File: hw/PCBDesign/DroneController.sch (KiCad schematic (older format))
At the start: 5 parts, among them J1 SerialDebug

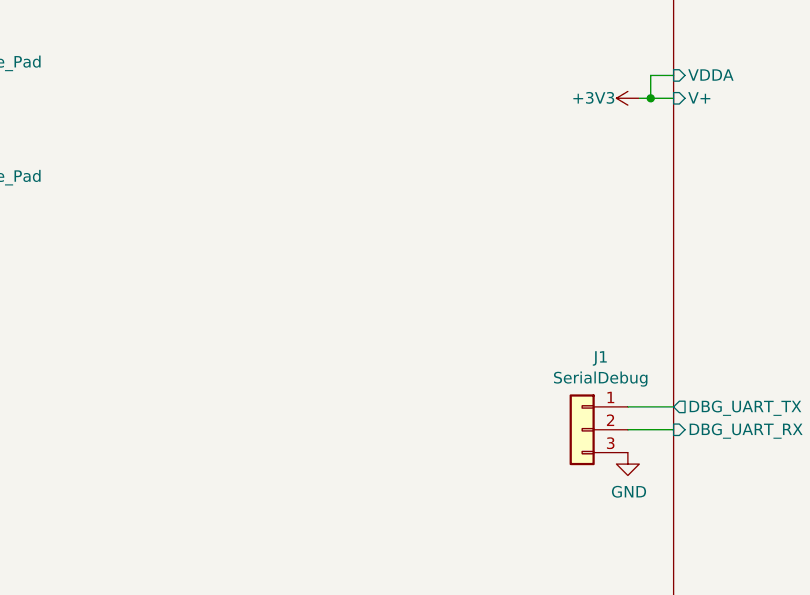
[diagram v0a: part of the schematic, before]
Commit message: Investigate some USB issues. Add PCB remarks for revision 2
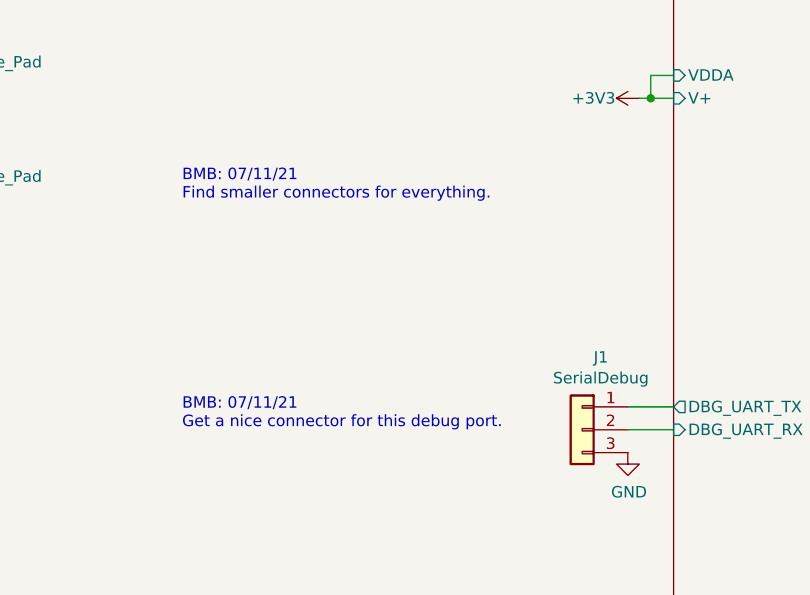
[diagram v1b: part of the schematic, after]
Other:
- note added: "BMB: 07/11/21\nFind smaller connectors for everything."
- note added: "BMB: 07/11/21\nGet a nice connector for this debug port."
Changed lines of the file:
@@
 Wire Wire Line
 	8050 1100 8000 1100
+Text Notes 2350 3700 0    50   ~ 0
+BMB: 07/11/21\nGet a nice connector for this debug port.
+Text Notes 2350 2700 0    50   ~ 0
+BMB: 07/11/21\nFind smaller connectors for everything.
 $EndSCHEMATC

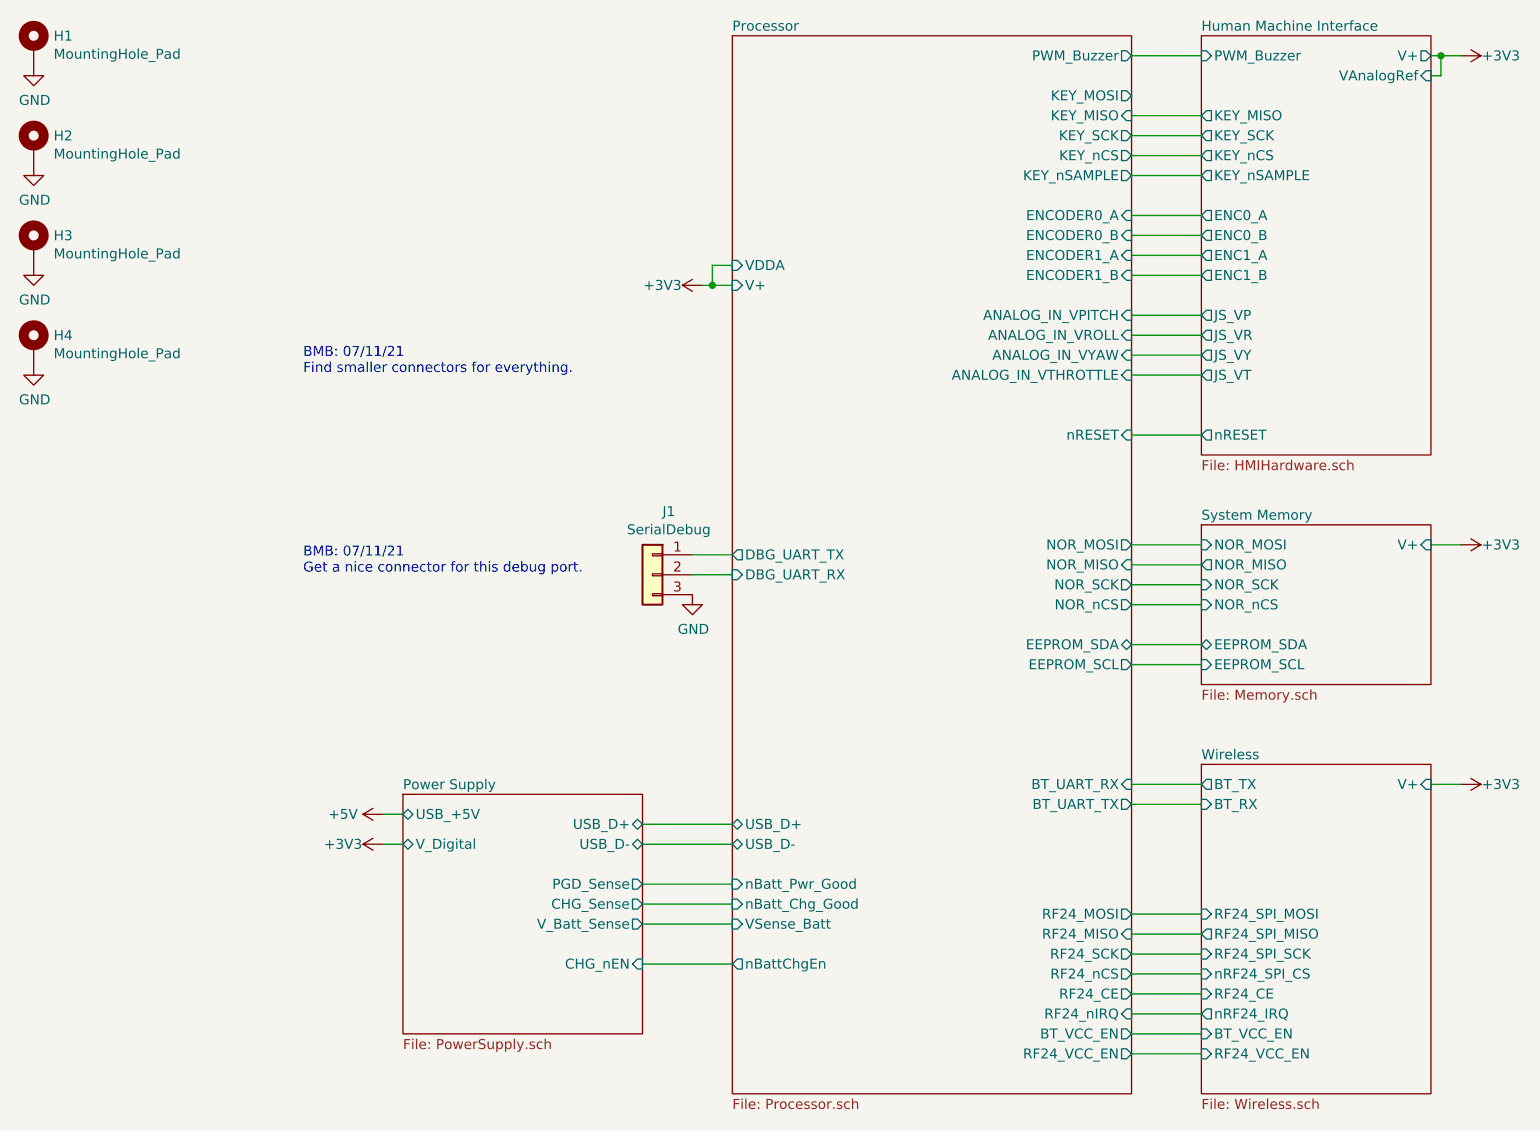
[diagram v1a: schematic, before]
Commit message: Start working on PCB rev 2.0
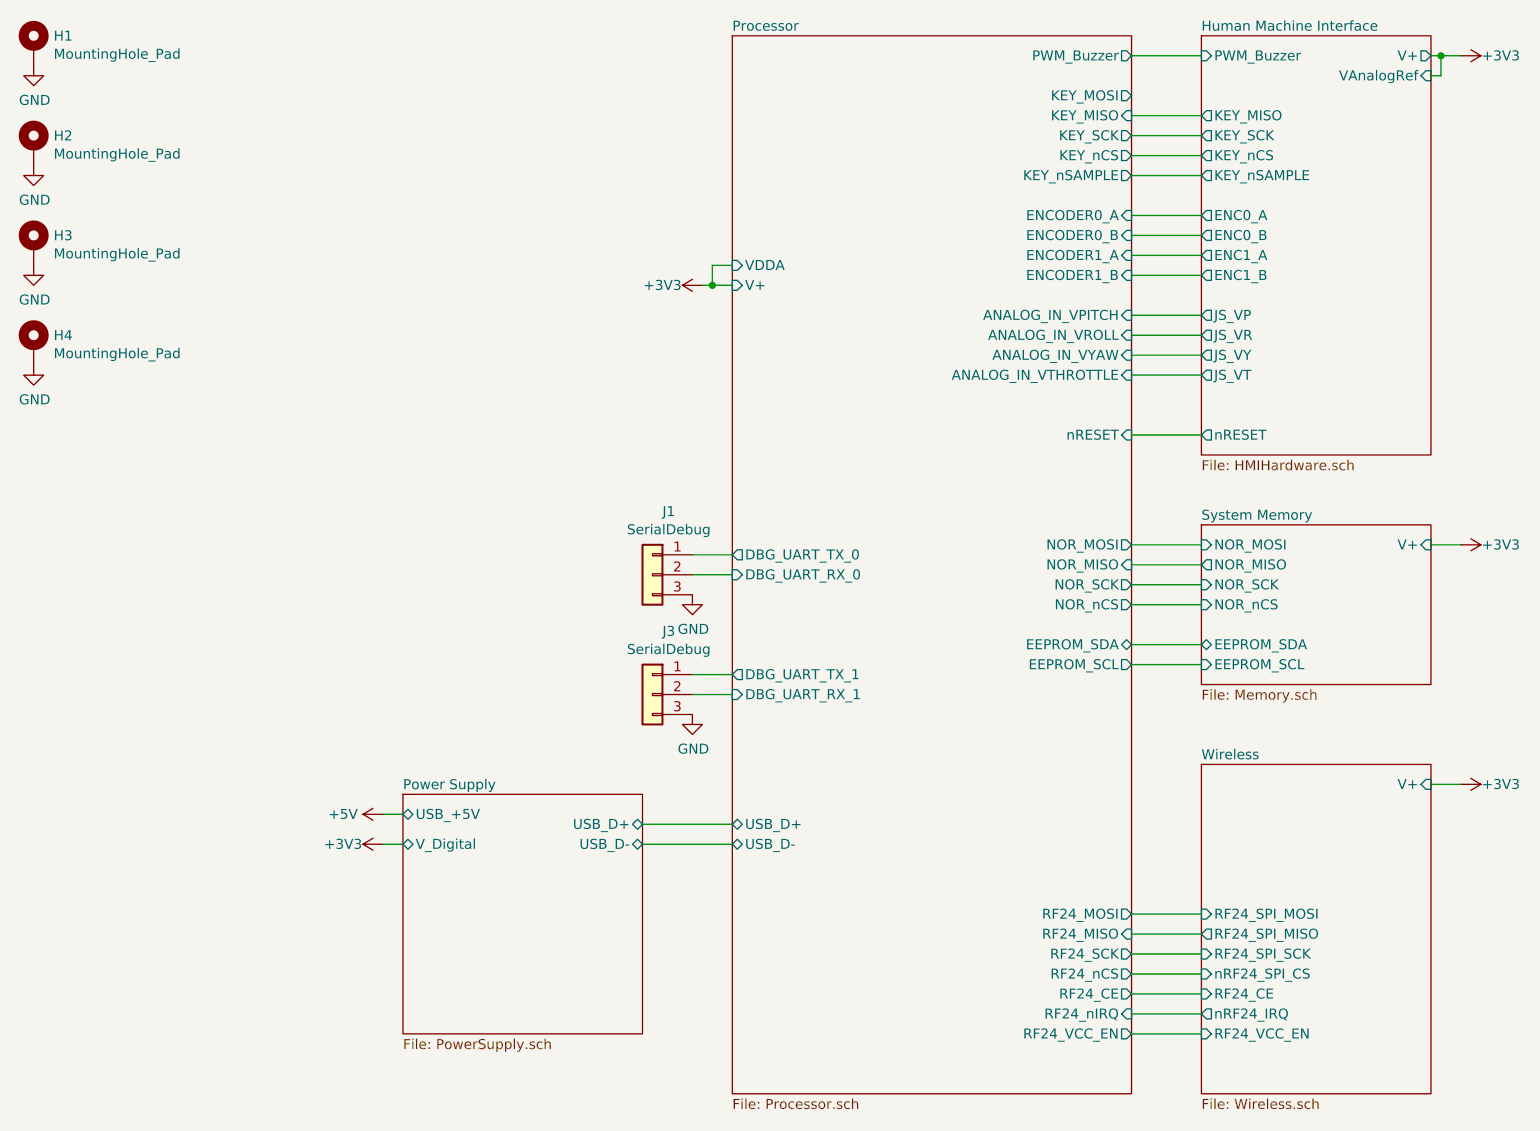
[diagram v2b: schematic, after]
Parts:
- added J3: SerialDebug, Connector_Molex:Molex_PicoBlade_53261-0371_1x03-1MP_P1.25mm_Horizontal, symbol Connector_Generic:Conn_01x03
- J1: footprint Connector_PinHeader_2.54mm:PinHeader_1x03_P2.54mm_Vertical -> Connector_Molex:Molex_PicoBlade_53261-0371_1x03-1MP_P1.25mm_Horizontal; DigiKey (none) -> WM7621CT-ND; Digikey (none) -> WM7621CT-ND
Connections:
- net GND: now also J3.3 (Pin_3)
- net Processor/DBG_UART_RX renamed Processor/DBG_UART_RX_0
- net Processor/DBG_UART_TX renamed Processor/DBG_UART_TX_0
- new net Processor/DBG_UART_RX_1: J3.2 (Pin_2)
- new net Processor/DBG_UART_TX_1: J3.1 (Pin_1)
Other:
- note removed: "BMB: 07/11/21\nFind smaller connectors for everything."
- note removed: "BMB: 07/11/21\nGet a nice connector for this debug port."
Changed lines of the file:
@@
 F0 "Wireless" 50
 F1 "Wireless.sch" 50
-F2 "BT_RX" I L 6850 4850 50
-F3 "BT_TX" O L 6850 4750 50
 F4 "RF24_SPI_MOSI" I L 6850 5400 50
 F5 "RF24_SPI_MISO" O L 6850 5500 50
@@
 F9 "nRF24_IRQ" O L 6850 5900 50
 F10 "V+" I R 8000 4750 50
-F11 "BT_VCC_EN" I L 6850 6000 50
-F12 "RF24_VCC_EN" I L 6850 6100 50
+F12 "RF24_VCC_EN" I L 6850 6000 50
 $EndSheet
 $Comp
@@
 F4 "USB_D-" B R 4050 5050 50
 F5 "USB_+5V" B L 2850 4900 50
-F6 "PGD_Sense" O R 4050 5250 50
-F7 "CHG_Sense" O R 4050 5350 50
-F8 "CHG_nEN" I R 4050 5650 50
-F9 "V_Batt_Sense" O R 4050 5450 50
 $EndSheet
 $Sheet
@@
 F2 "USB_D+" B L 4500 4950 50
 F3 "USB_D-" B L 4500 5050 50
-F4 "nBatt_Pwr_Good" I L 4500 5250 50
-F5 "nBatt_Chg_Good" I L 4500 5350 50
-F6 "nBattChgEn" O L 4500 5650 50
-F7 "BT_UART_RX" I R 6500 4750 50
-F8 "BT_UART_TX" O R 6500 4850 50
-F9 "RF24_MOSI" O R 6500 5400 50
-F10 "RF24_MISO" I R 6500 5500 50
-F11 "RF24_SCK" O R 6500 5600 50
-F12 "RF24_nCS" O R 6500 5700 50
-F13 "RF24_CE" O R 6500 5800 50
-F14 "RF24_nIRQ" I R 6500 5900 50
-F15 "NOR_MOSI" O R 6500 3550 50
-F16 "NOR_MISO" I R 6500 3650 50
-F17 "NOR_SCK" O R 6500 3750 50
-F18 "NOR_nCS" O R 6500 3850 50
-F19 "EEPROM_SDA" B R 6500 4050 50
-F20 "EEPROM_SCL" O R 6500 4150 50
-F21 "V+" I L 4500 2250 50
-F22 "nRESET" I R 6500 3000 50
-F23 "PWM_Buzzer" O R 6500 1100 50
-F24 "KEY_MOSI" O R 6500 1300 50
-F25 "KEY_MISO" I R 6500 1400 50
-F26 "KEY_SCK" O R 6500 1500 50
-F27 "KEY_nCS" O R 6500 1600 50
-F28 "KEY_nSAMPLE" O R 6500 1700 50
-F29 "ENCODER0_A" I R 6500 1900 50
-F30 "ENCODER0_B" I R 6500 2000 50
-F31 "ENCODER1_A" I R 6500 2100 50
-F32 "ENCODER1_B" I R 6500 2200 50
-F33 "ANALOG_IN_VPITCH" I R 6500 2400 50
-F34 "ANALOG_IN_VROLL" I R 6500 2500 50
-F35 "ANALOG_IN_VYAW" I R 6500 2600 50
-F36 "ANALOG_IN_VTHROTTLE" I R 6500 2700 50
-F37 "VDDA" I L 4500 2150 50
-F38 "DBG_UART_TX" O L 4500 3600 50
-F39 "DBG_UART_RX" I L 4500 3700 50
-F40 "BT_VCC_EN" O R 6500 6000 50
-F41 "RF24_VCC_EN" O R 6500 6100 50
-F42 "VSense_Batt" I L 4500 5450 50
+F4 "RF24_MOSI" O R 6500 5400 50
+F5 "RF24_MISO" I R 6500 5500 50
+F6 "RF24_SCK" O R 6500 5600 50
+F7 "RF24_nCS" O R 6500 5700 50
+F8 "RF24_CE" O R 6500 5800 50
+F9 "RF24_nIRQ" I R 6500 5900 50
+F10 "NOR_MOSI" O R 6500 3550 50
+F11 "NOR_MISO" I R 6500 3650 50
+F12 "NOR_SCK" O R 6500 3750 50
+F13 "NOR_nCS" O R 6500 3850 50
+F14 "EEPROM_SDA" B R 6500 4050 50
+F15 "EEPROM_SCL" O R 6500 4150 50
+F16 "V+" I L 4500 2250 50
+F17 "nRESET" I R 6500 3000 50
+F18 "PWM_Buzzer" O R 6500 1100 50
+F19 "KEY_MOSI" O R 6500 1300 50
+F20 "KEY_MISO" I R 6500 1400 50
+F21 "KEY_SCK" O R 6500 1500 50
+F22 "KEY_nCS" O R 6500 1600 50
+F23 "KEY_nSAMPLE" O R 6500 1700 50
+F24 "ENCODER0_A" I R 6500 1900 50
+F25 "ENCODER0_B" I R 6500 2000 50
+F26 "ENCODER1_A" I R 6500 2100 50
+F27 "ENCODER1_B" I R 6500 2200 50
+F28 "ANALOG_IN_VPITCH" I R 6500 2400 50
+F29 "ANALOG_IN_VROLL" I R 6500 2500 50
+F30 "ANALOG_IN_VYAW" I R 6500 2600 50
+F31 "ANALOG_IN_VTHROTTLE" I R 6500 2700 50
+F32 "VDDA" I L 4500 2150 50
+F33 "RF24_VCC_EN" O R 6500 6000 50
+F34 "DBG_UART_RX_1" I L 4500 4300 50
+F35 "DBG_UART_TX_1" O L 4500 4200 50
+F36 "DBG_UART_TX_0" O L 4500 3600 50
+F37 "DBG_UART_RX_0" I L 4500 3700 50
 $EndSheet
 Wire Wire Line
 	8150 4750 8000 4750
 Wire Wire Line
-	6500 4750 6850 4750
-Wire Wire Line
-	6500 4850 6850 4850
-Wire Wire Line
 	6500 5400 6850 5400
 Wire Wire Line
@@
 Wire Wire Line
 	4050 5050 4500 5050
-Wire Wire Line
-	4050 5250 4500 5250
-Wire Wire Line
-	4050 5350 4500 5350
-Wire Wire Line
-	4050 5450 4500 5450
-Wire Wire Line
-	4050 5650 4500 5650
 $Comp
 L power:+3V3 #PWR011
@@
 	6500 2200 6850 2200
 Wire Wire Line
-	6500 6000 6850 6000
-Wire Wire Line
-	6500 6100 6850 6100
-Wire Wire Line
 	4300 3600 4500 3600
 Wire Wire Line
@@
 F 0 "J1" H 4018 4017 50  0000 C CNN
 F 1 "SerialDebug" H 4018 3926 50  0000 C CNN
-F 2 "Connector_PinHeader_2.54mm:PinHeader_1x03_P2.54mm_Vertical" H 4100 3700 50  0001 C CNN
+F 2 "Connector_Molex:Molex_PicoBlade_53261-0371_1x03-1MP_P1.25mm_Horizontal" H 4100 3700 50  0001 C CNN
 F 3 "~" H 4100 3700 50  0001 C CNN
+F 4 "WM7621CT-ND" H 4100 3700 50  0001 C CNN "DigiKey"
+F 5 "WM7621CT-ND" H 4100 3700 50  0001 C CNN "Digikey"
 	1    4100 3700
 	-1   0    0    -1
@@
 Wire Wire Line
 	8050 1100 8000 1100
-Text Notes 2350 3700 0    50   ~ 0
-BMB: 07/11/21\nGet a nice connector for this debug port.
-Text Notes 2350 2700 0    50   ~ 0
-BMB: 07/11/21\nFind smaller connectors for everything.
+$Comp
+L Connector_Generic:Conn_01x03 J3
+U 1 1 61CEB0C2
+P 4100 4300
+F 0 "J3" H 4018 4617 50  0000 C CNN
+F 1 "SerialDebug" H 4018 4526 50  0000 C CNN
+F 2 "Connector_Molex:Molex_PicoBlade_53261-0371_1x03-1MP_P1.25mm_Horizontal" H 4100 4300 50  0001 C CNN
+F 3 "~" H 4100 4300 50  0001 C CNN
+F 4 "WM7621CT-ND" H 4100 4300 50  0001 C CNN "DigiKey"
+F 5 "WM7621CT-ND" H 4100 4300 50  0001 C CNN "Digikey"
+	1    4100 4300
+	-1   0    0    -1
+$EndComp
+Wire Wire Line
+	6500 6000 6850 6000
+$Comp
+L power:GND #PWR07
+U 1 1 61D5E366
+P 4300 4400
+F 0 "#PWR07" H 4300 4150 50  0001 C CNN
+F 1 "GND" H 4305 4227 50  0000 C CNN
+F 2 "" H 4300 4400 50  0001 C CNN
+F 3 "" H 4300 4400 50  0001 C CNN
+	1    4300 4400
+	1    0    0    -1
+$EndComp
+Wire Wire Line
+	4300 4300 4500 4300
+Wire Wire Line
+	4300 4200 4500 4200
 $EndSCHEMATC

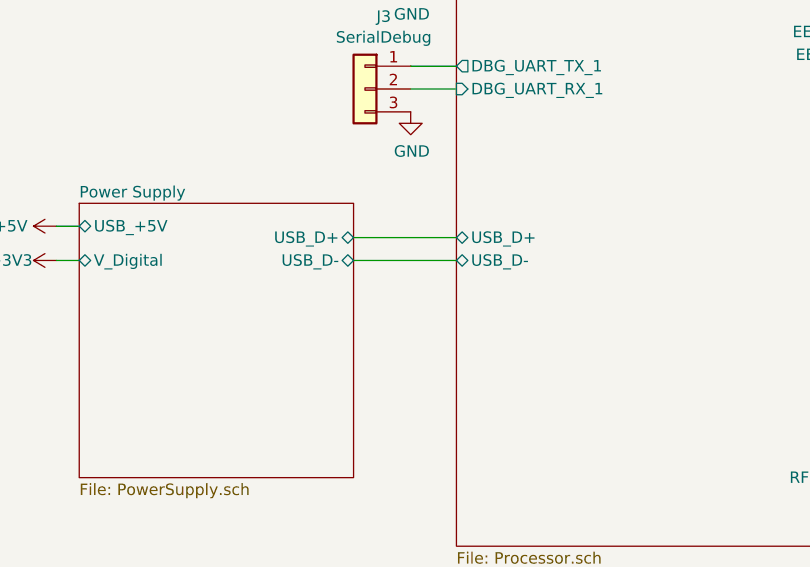
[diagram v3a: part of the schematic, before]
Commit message: Work further on v2.0 of controller pcb
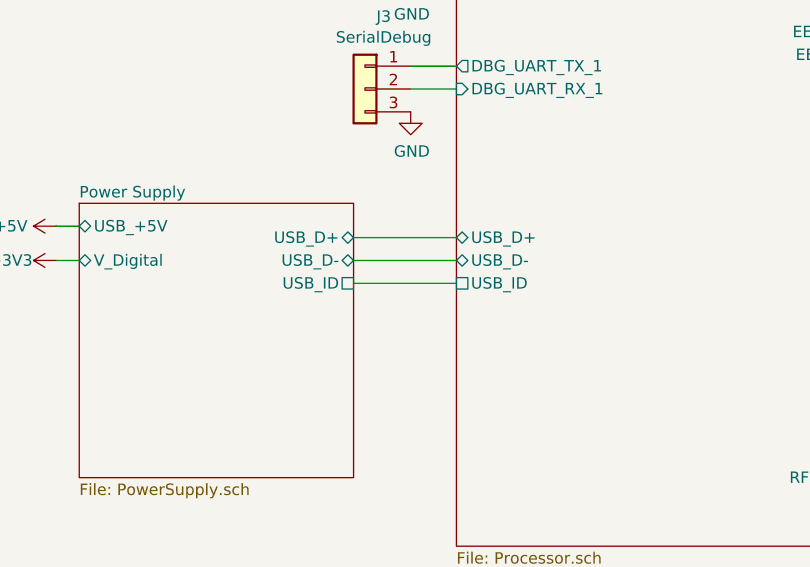
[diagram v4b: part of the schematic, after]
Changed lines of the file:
@@
 F4 "USB_D-" B R 4050 5050 50
 F5 "USB_+5V" B L 2850 4900 50
+F6 "USB_ID" U R 4050 5150 50
 $EndSheet
 $Sheet
@@
 F36 "DBG_UART_TX_0" O L 4500 3600 50
 F37 "DBG_UART_RX_0" I L 4500 3700 50
+F38 "USB_ID" U L 4500 5150 50
 $EndSheet
 Wire Wire Line
@@
 Wire Wire Line
 	4300 4200 4500 4200
+Wire Wire Line
+	4050 5150 4500 5150
 $EndSCHEMATC

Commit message: Finish first draft of v2.0 pcb
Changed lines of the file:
@@
 $Descr A4 11693 8268
 encoding utf-8
-Sheet 1 11
+Sheet 1 10
 Title ""
 Date ""
@@
 F0 "Human Machine Interface" 50
 F1 "HMIHardware.sch" 50
-F2 "PWM_Buzzer" I L 6850 1100 50
 F3 "KEY_MISO" O L 6850 1400 50
 F4 "KEY_SCK" O L 6850 1500 50
@@
 F16 "V+" I L 4500 2250 50
 F17 "nRESET" I R 6500 3000 50
-F18 "PWM_Buzzer" O R 6500 1100 50
-F19 "KEY_MOSI" O R 6500 1300 50
 F20 "KEY_MISO" I R 6500 1400 50
 F21 "KEY_SCK" O R 6500 1500 50
@@
 	6500 2400 6850 2400
 Wire Wire Line
-	6500 1100 6850 1100
-Wire Wire Line
 	6500 1400 6850 1400
